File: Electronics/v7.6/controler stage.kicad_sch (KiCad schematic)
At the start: 28 parts, among them IC4 RTC PCF8523T, J1 Conn_02x03_Odd_Even, SW2 SPST_TACT-KMR2, U1 ATSAMD21G18A, U4 Adafruit LCD Screen, X1 ClockXtal, X2 uXtal, X4 microsd

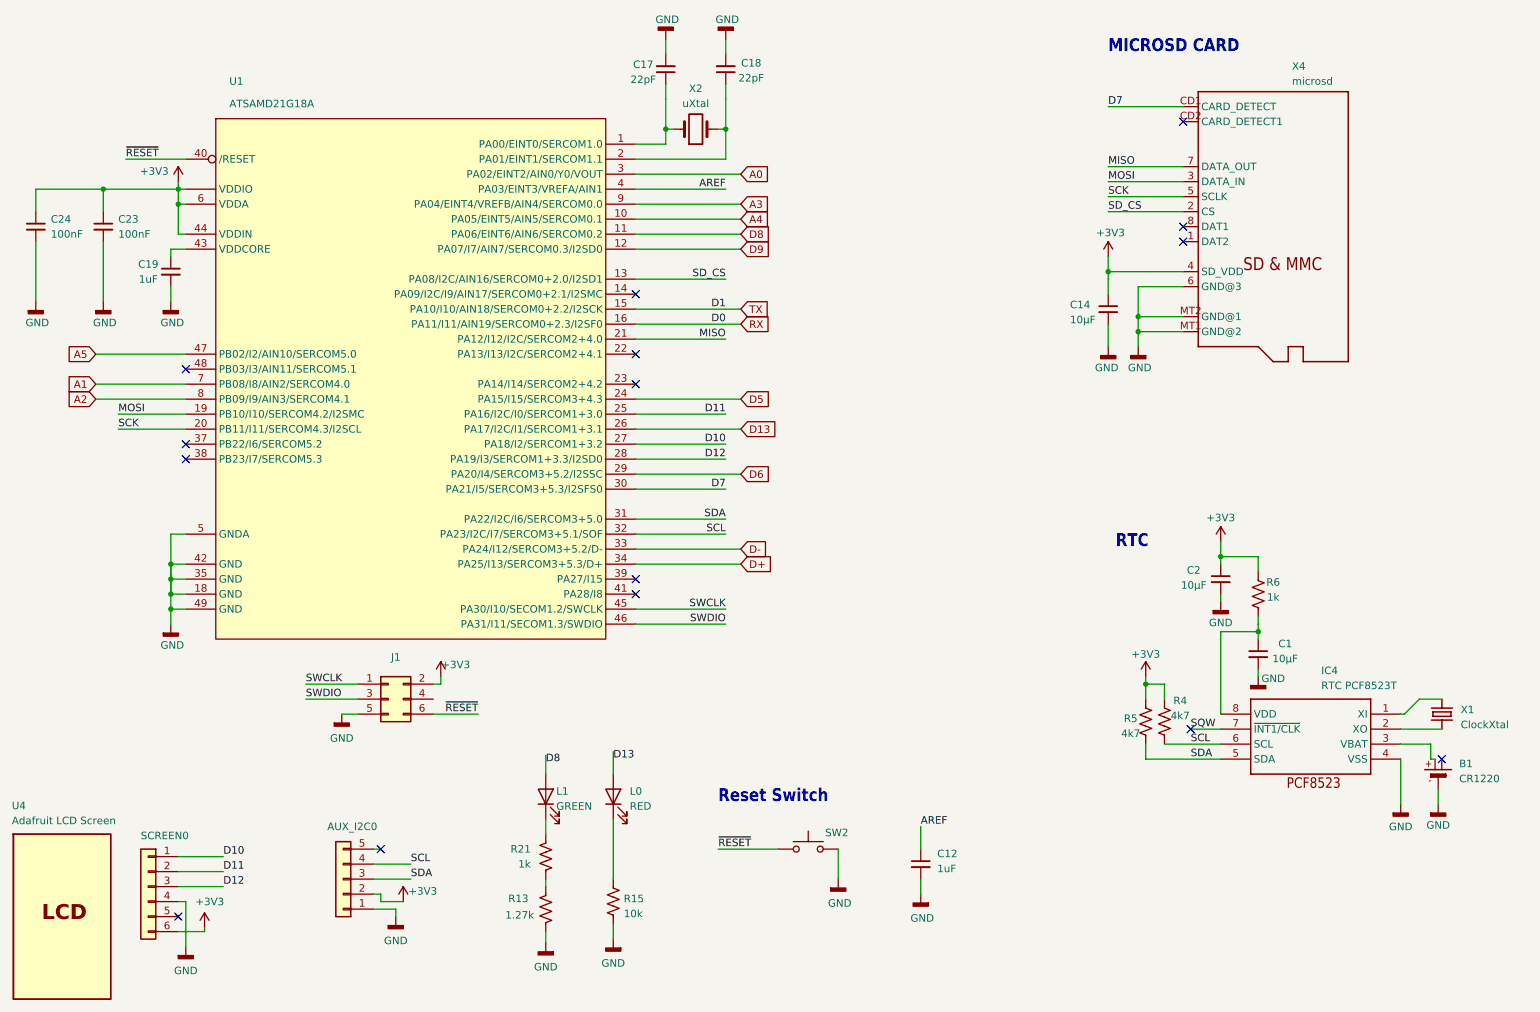
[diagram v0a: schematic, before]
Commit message: Add D2.0mm testpoints and PCB fixes
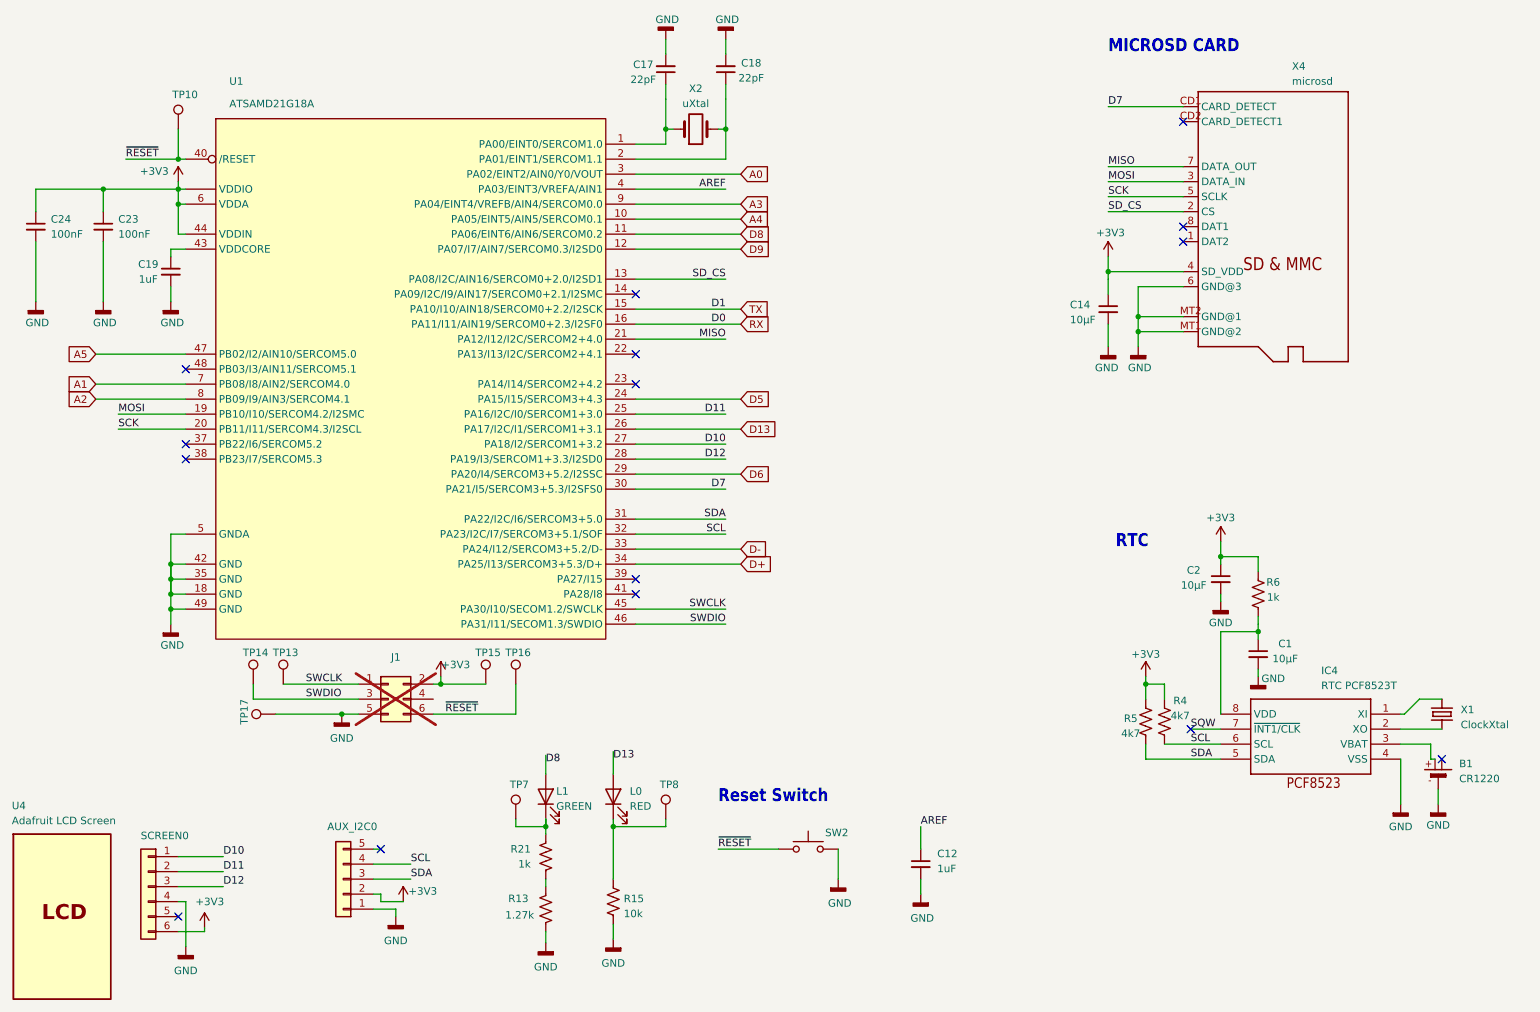
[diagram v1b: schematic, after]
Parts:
- added TP10, TP7, TP8: 3V3, TestPoint:TestPoint_Pad_D2.0mm, symbol Connector:TestPoint
- added TP13, TP14, TP15, TP16, TP17: GND, TestPoint:TestPoint_Pad_D2.0mm, symbol Connector:TestPoint
- J1: now not fitted
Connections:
- net +3V3: now also TP15.1
- net GND: now also TP17.1
- net SWCLK: now also TP13.1
- net SWDIO: now also TP14.1
- net ~{RESET}: now also TP10.1, TP16.1
- net at L1.1 (K), R21.2: now also TP7.1
- net at L0.1 (K), R15.1: now also TP8.1
